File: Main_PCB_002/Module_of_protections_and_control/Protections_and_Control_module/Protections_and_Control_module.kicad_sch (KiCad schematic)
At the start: 52 parts

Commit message: Control & Protections board
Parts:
- removed D?: WireHole_1p5, libraries:WireHole_1p2, symbol Connectors_for_Wire:WireHole_1p5
- added C1, C11, C13, C3, C6, C7, C8: C, Capacitor_SMD:C_1206_3216Metric_Pad1.33x1.80mm_HandSolder, symbol Device:C
- added D16, D17, D18, D2: WireHole_1p5, libraries:WireHole_1p2, symbol Connectors_for_Wire:WireHole_1p5
- C10, C12, C2, C4, C5, C9: renamed from C?; footprint (none) -> Capacitor_SMD:C_1206_3216Metric_Pad1.33x1.80mm_HandSolder
- C14: renamed from C?; footprint Capacitor_SMD:C_1812_4532Metric_Pad1.57x3.40mm_HandSolder -> (none)
- D10, D11, D12, D13, D14: renamed from D?; footprint libraries:WireHole_1p2 -> (none)
- L1, L2, L3, L4, L5, L6, L7, L8: renamed from L?; footprint libraries:INDC2016X80N -> (none)
- Q1, Q2, Q5, Q6: renamed from Q?; footprint DFN_3X3_EP -> libraries:DFN_3X3_EP
- gave numbers to parts that had none: 27
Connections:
- net GND: now also C2.2, D4.1 (Conn), D7.2 (A), Q1.5 (D_1), Q1.6 (D_2), Q1.7 (D_3), Q1.8 (D_4), Q2.5 (D_1), Q2.6 (D_2), Q2.7 (D_3), Q2.8 (D_4), R2.2, C1.2, D16.1 (Conn), D17.1 (Conn), D18.1 (Conn), D2.1 (Conn)
- net at C5.1, L3.2, L5.1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: now also C6.1
- net at C12.1, D13.1 (Conn), L5.2: now also C13.1
- net at C4.1, L1.2, L3.1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: now also C3.1
- net at C4.2, C5.2, C9.2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: now also C3.2, C6.2; no longer D4.1 (Conn), Q1.5 (D_1), Q1.6 (D_2), Q1.7 (D_3), Q1.8 (D_4)
- net at C10.1, D10.1 (Conn), L4.2: now also C11.1
- net at C2.1, D6.1 (K), L2.2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: now also C1.1, C7.1, C8.1
- net at D9.2 (A), Q2.1 (S_1), Q2.2 (S_2)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: now also C7.2, C8.2
- net at C12.2, D12.1 (Conn), Q6.5 (D_1)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: now also C13.2
- net at C10.2, D11.1 (Conn), Q5.5 (D_1)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: now also C11.2
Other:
- moved on the sheet: C2, C4, D10, D11, D12, D13, D4, D9, L4, Q4, Q5, R4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

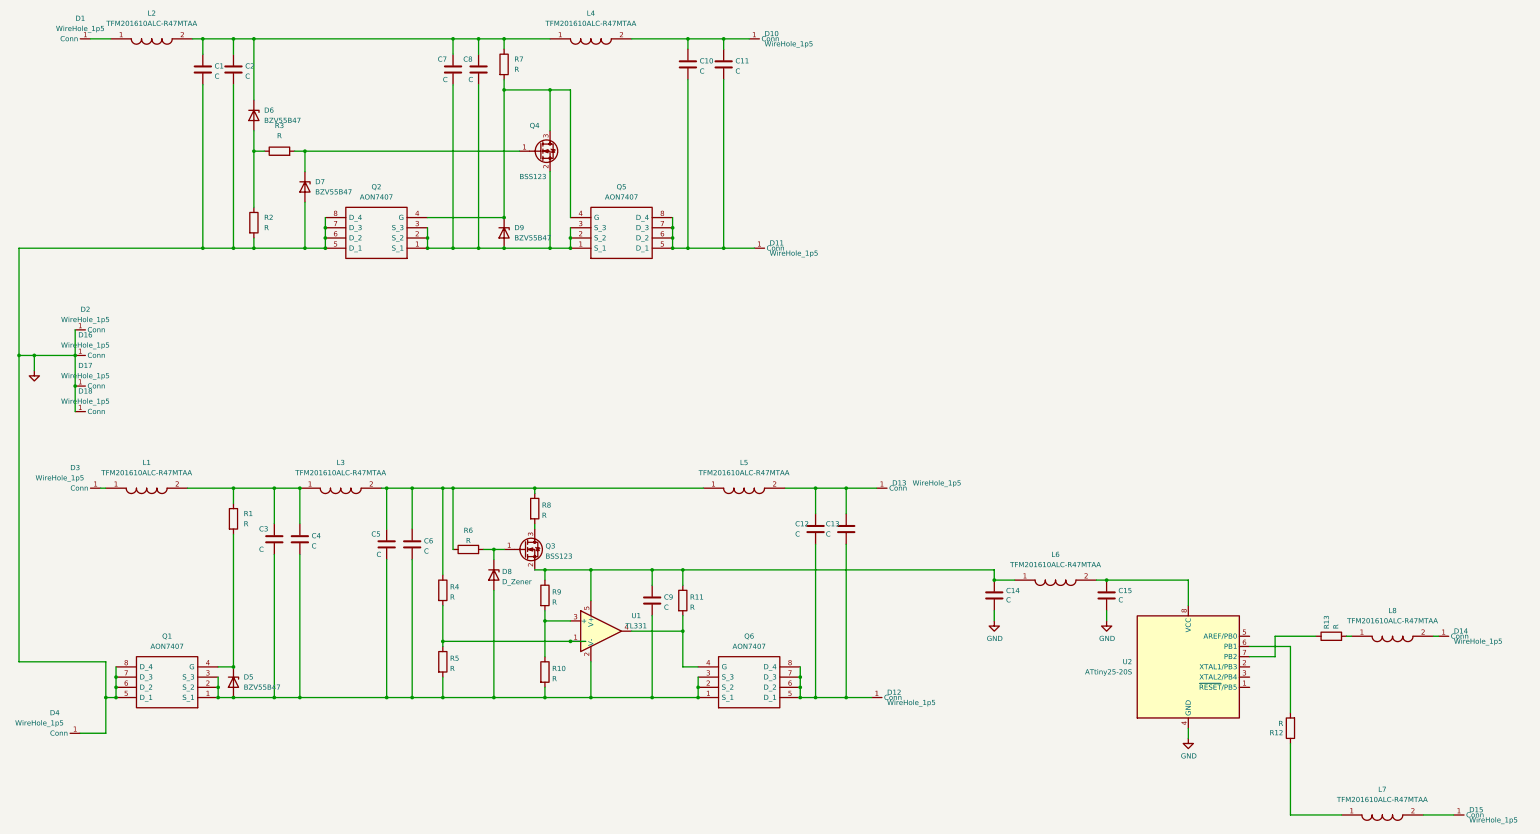
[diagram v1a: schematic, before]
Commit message: Module of protections and control
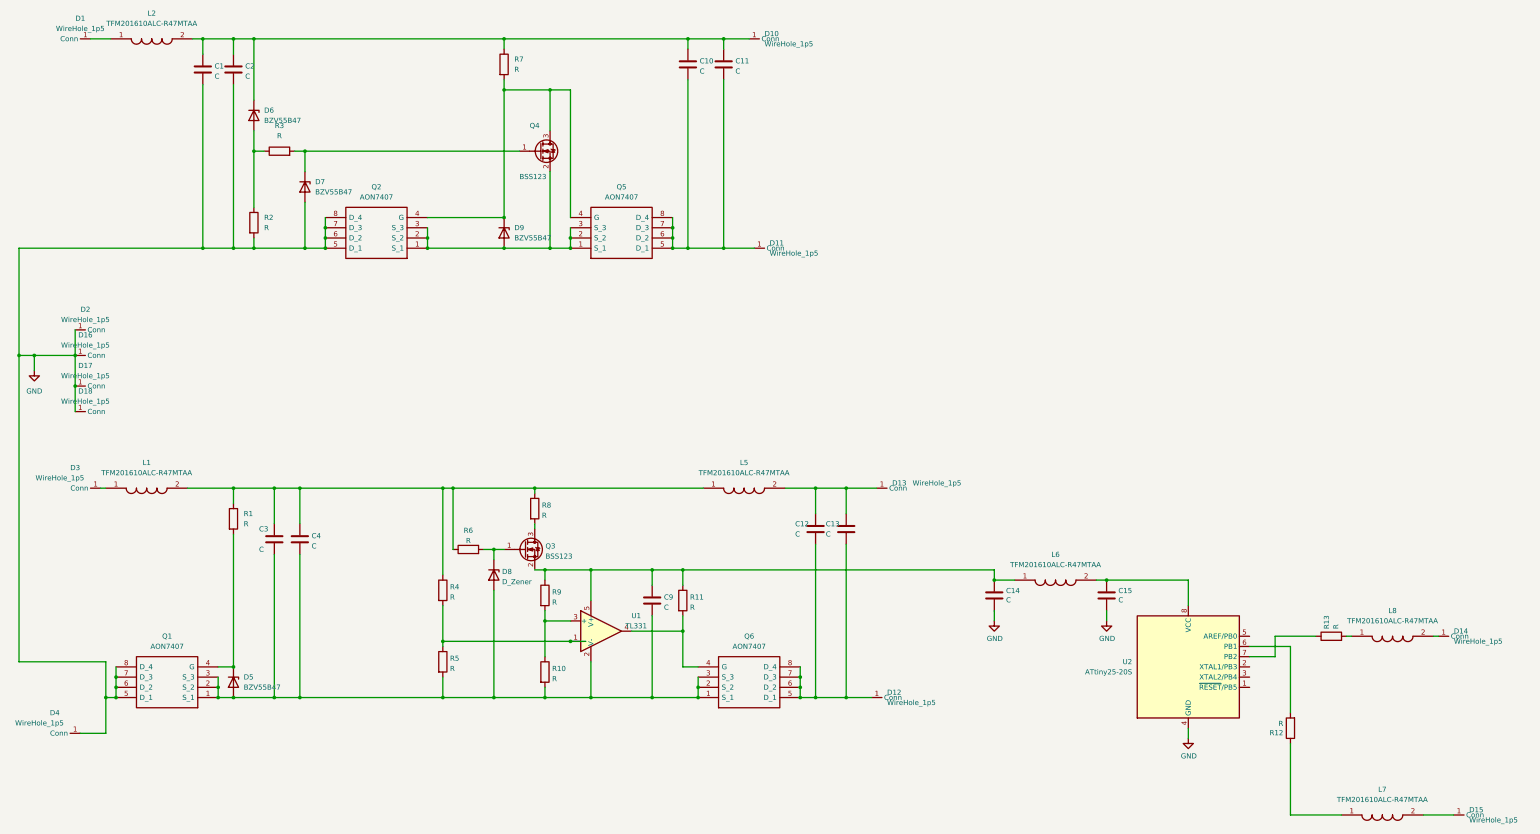
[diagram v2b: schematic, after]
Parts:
- removed C5, C6, C7, C8: C, Capacitor_SMD:C_1206_3216Metric_Pad1.33x1.80mm_HandSolder, symbol Device:C
- removed L3, L4: TFM201610ALC-R47MTAA, symbol TFM201610ALC-R47MTAA:TFM201610ALC-R47MTAA
- C1, C10, C12, C3: footprint Capacitor_SMD:C_1206_3216Metric_Pad1.33x1.80mm_HandSolder -> (none)
- C14: footprint (none) -> Capacitor_SMD:C_0603_1608Metric_Pad1.08x0.95mm_HandSolder
- D5, D6, D7, D9: footprint Diode_SMD:D_MiniMELF -> (none)
- D8: footprint (none) -> libraries:SOD2513X120N
- L1, L2, L5: footprint (none) -> libraries:INDPM4442X200N
- L6, L7, L8: footprint (none) -> libraries:INDC2112X105N
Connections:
- net at L5.1, R4.1, R6.1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: now also C3.1, C4.1, L1.2, R1.1
- net at C1.1, C2.1, D6.1 (K)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: now also C10.1, C11.1, D10.1 (Conn)

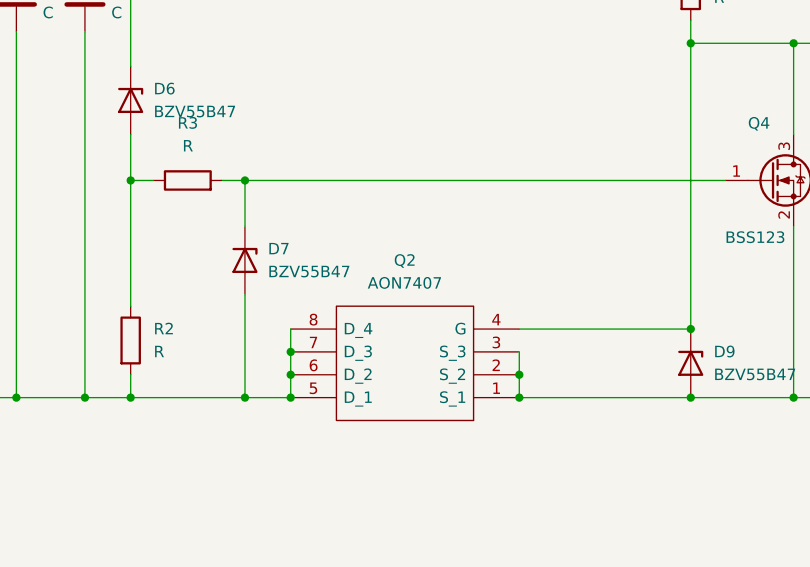
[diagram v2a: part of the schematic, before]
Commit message: Module of protections and control
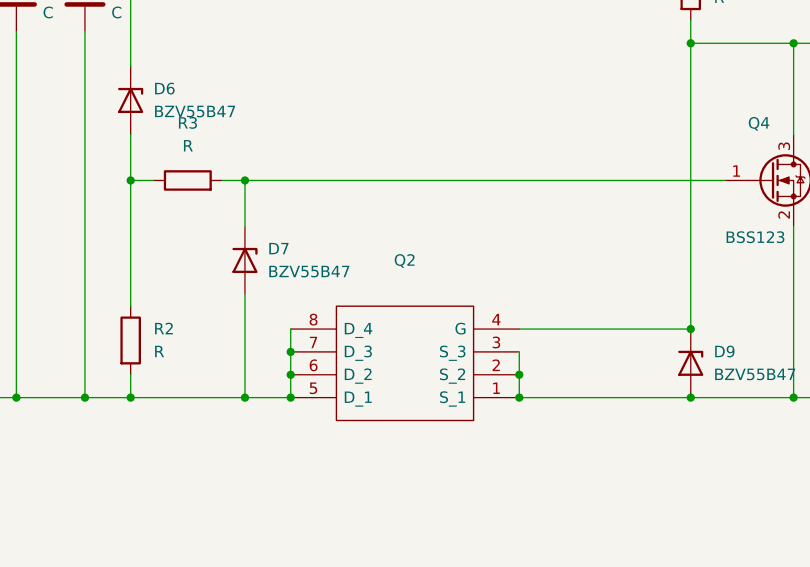
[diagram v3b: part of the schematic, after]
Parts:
- Q2: value AON7407 -> (none); footprint libraries:DFN_3X3_EP -> (none)
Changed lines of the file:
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@@
     (in_bom yes) (on_board yes) (fields_autoplaced)
     (property "Reference" "Q2" (id 0) (at 105.41 77.47 0))
-    (property "Value" "AON7407" (id 1) (at 105.41 80.01 0))
-    (property "Footprint" "libraries:DFN_3X3_EP" (id 2) (at 96.52 95.25 0)
+    (property "Value" "" (id 1) (at 105.41 80.01 0))
+    (property "Footprint" "" (id 2) (at 96.52 95.25 0)
       (effects (font (size 1.27 1.27)) (justify left) hide)
     )
